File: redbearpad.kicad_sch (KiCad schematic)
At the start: 11 parts, among them J1 BlendMicro_fila_izq, J2 BlendMicro_fila_der, J3 OLED_128x32_I2C, SW1 Redragon_LP, SW2 Redragon_LP, SW3 Redragon_LP, SW4 Redragon_LP, SW5 Redragon_LP, SW6 Redragon_LP, SW7 Redragon_LP, SW8 Redragon_LP

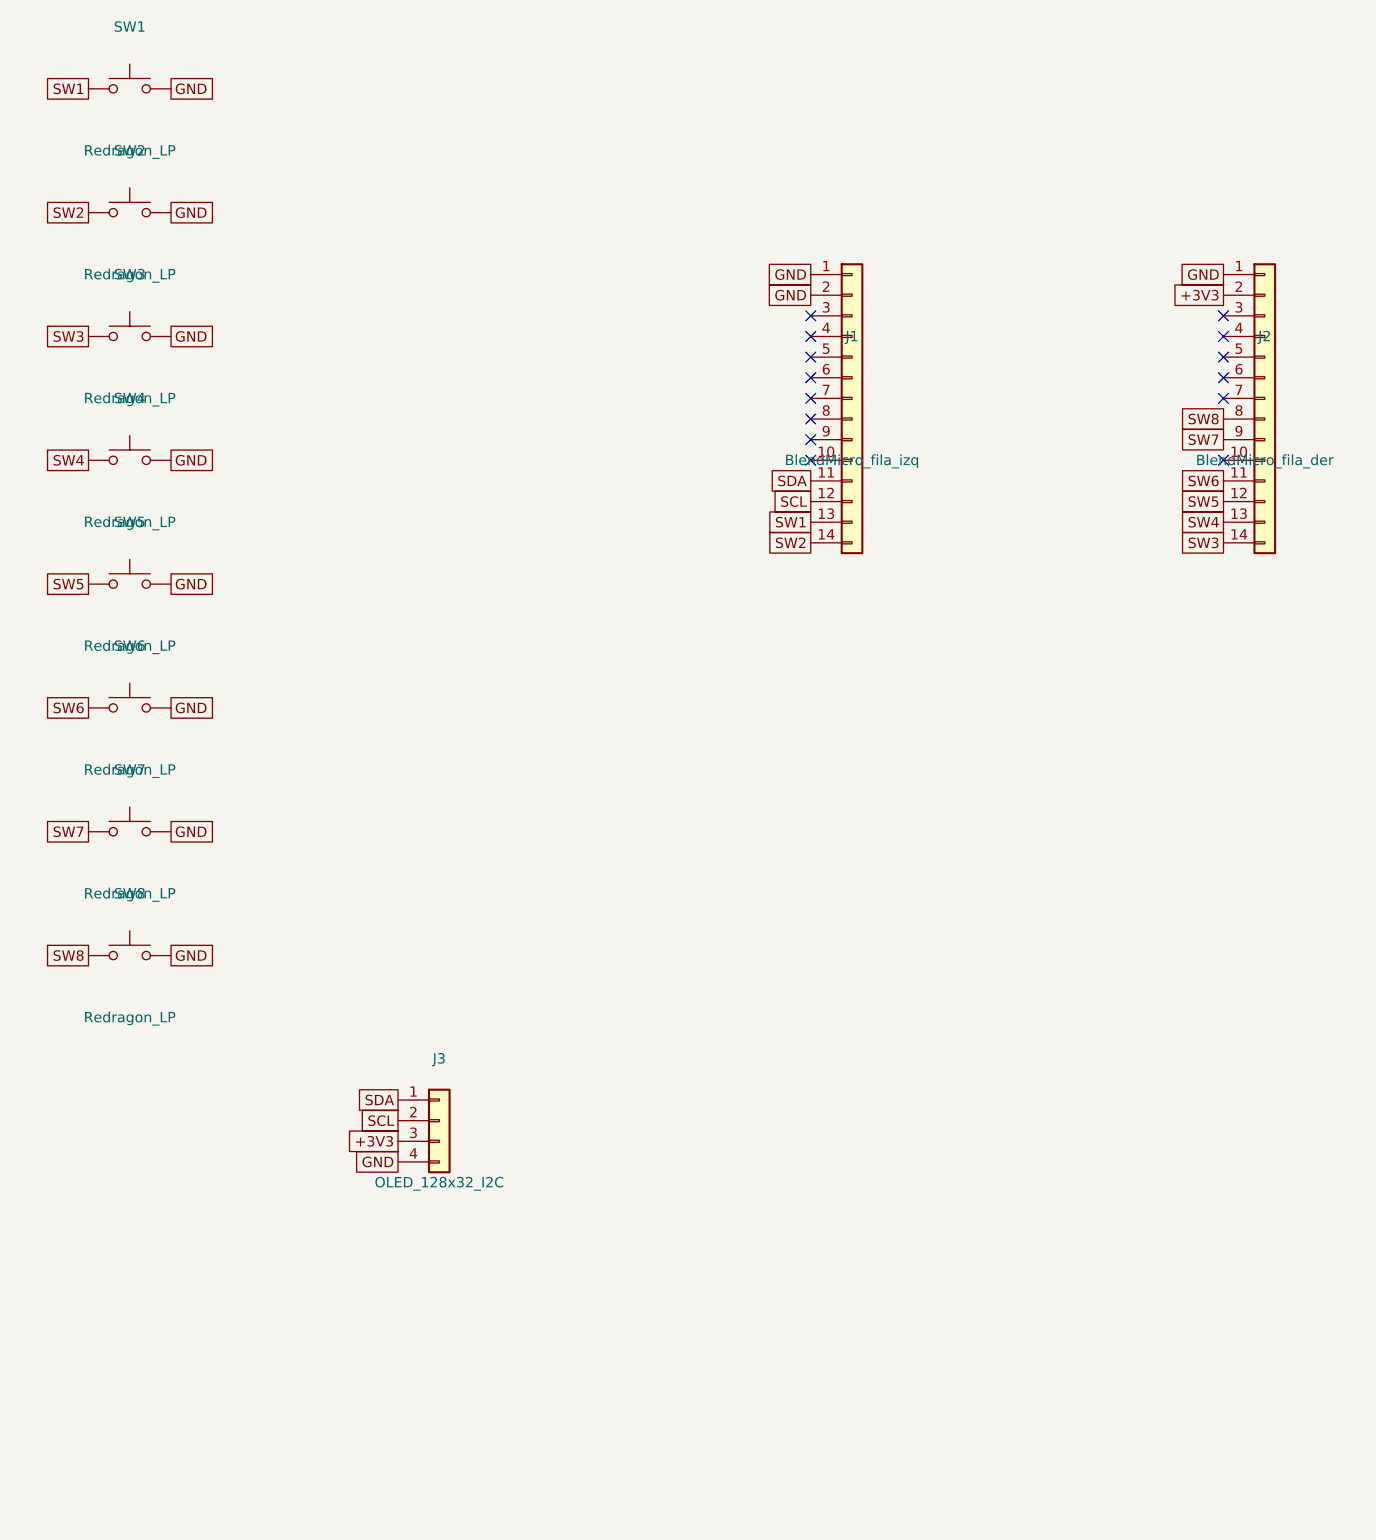
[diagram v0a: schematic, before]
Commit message: feat(pcb-v2): esquematico a 12 entradas (10 MX + 2 tact), OLED fuera
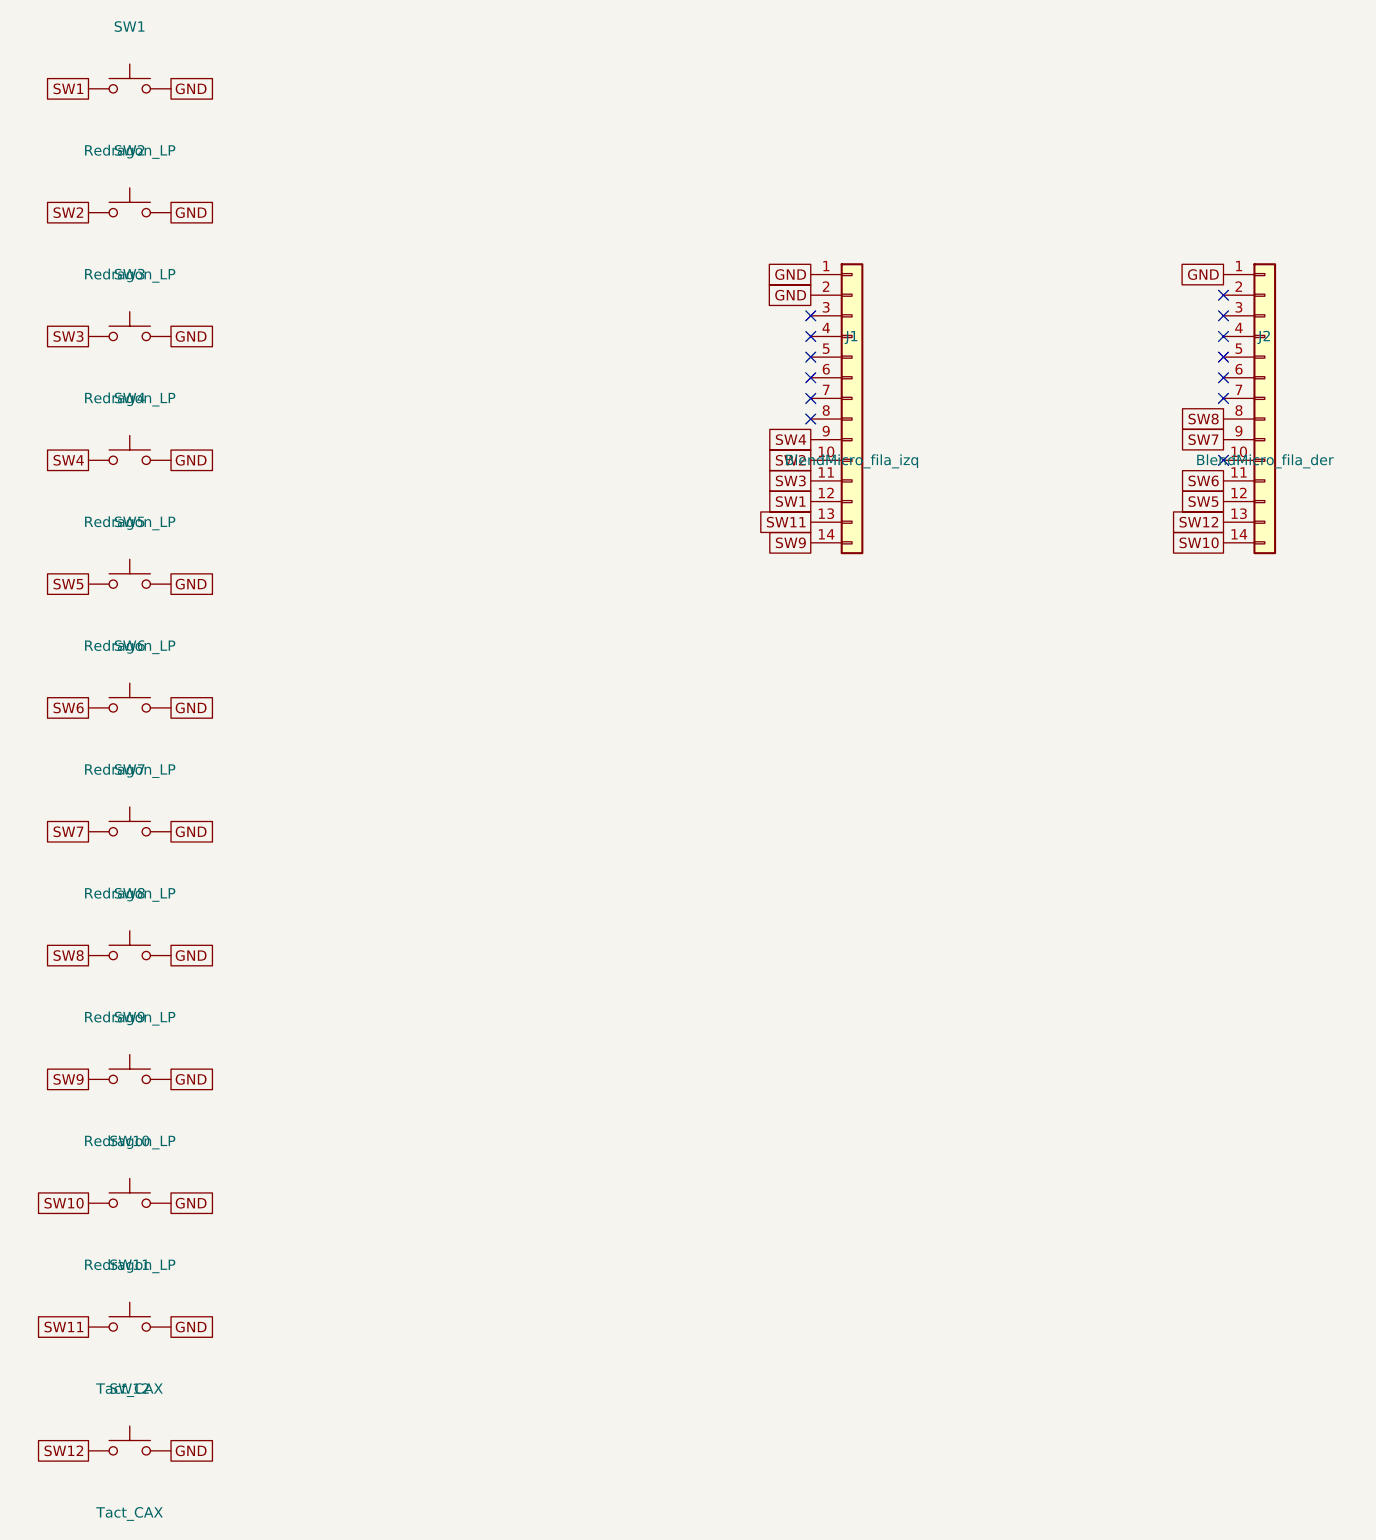
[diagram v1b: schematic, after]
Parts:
- removed J3: OLED_128x32_I2C, Connector_PinSocket_2.54mm:PinSocket_1x04_P2.54mm_Vertical, symbol Connector_Generic:Conn_01x04
- added SW10, SW9: Redragon_LP, redbearpad:SW_Redragon_LowProfile_PCB_1.00u, symbol Switch:SW_Push
- added SW11, SW12: Tact_CAX, redbearpad:SW_Tact_CAX_4.5x4.5, symbol Switch:SW_Push
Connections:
- net SCL is gone; now on net SW1: J1.12 (Pin_12)
- net SDA is gone; now on net SW3: J1.11 (Pin_11)
- net GND: now also SW10.2, SW11.2, SW12.2, SW9.2
- net SW1: no longer J1.13 (Pin_13)
- net SW2: now also J1.10 (Pin_10); no longer J1.14 (Pin_14)
- net SW3: no longer J2.14 (Pin_14)
- net SW4: now also J1.9 (Pin_9); no longer J2.13 (Pin_13)
- net +3V3: no longer names the net of J2.2 (Pin_2)
- new net SW10: J2.14 (Pin_14), SW10.1
- new net SW11: J1.13 (Pin_13), SW11.1
- new net SW12: J2.13 (Pin_13), SW12.1
- new net SW9: J1.14 (Pin_14), SW9.1
- no-connect marks 14 -> 13
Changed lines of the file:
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@@
   (global_label "SW8" (shape passive) (at 58.42 132.08 180) (effects (font (size 1.27 1.27)) (justify right)))
   (global_label "GND" (shape passive) (at 68.58 132.08 0) (effects (font (size 1.27 1.27)) (justify left)))
+  (symbol (lib_id "Switch:SW_Push") (at 63.5 147.32 0) (unit 1)
+    (exclude_from_sim no) (in_bom yes) (on_board yes) (dnp no)
+    (property "Reference" "SW9" (at 63.5 139.7 0) (effects (font (size 1.27 1.27))))
+    (property "Value" "Redragon_LP" (at 63.5 154.94 0) (effects (font (size 1.27 1.27))))
+    (property "Footprint" "redbearpad:SW_Redragon_LowProfile_PCB_1.00u" (at 63.5 147.32 0) (effects (font (size 1.27 1.27)) (hide yes)))
+    (property "Datasheet" "" (at 63.5 147.32 0) (effects (font (size 1.27 1.27)) (hide yes)))
+    (pin "1")
+    (pin "2")
+    (instances (project "redbearpad" (path "/f0a11111-2222-3333-4444-555566667777" (reference "SW9") (unit 1))))
+  )
+  (global_label "SW9" (shape passive) (at 58.42 147.32 180) (effects (font (size 1.27 1.27)) (justify right)))
+  (global_label "GND" (shape passive) (at 68.58 147.32 0) (effects (font (size 1.27 1.27)) (justify left)))
+  (symbol (lib_id "Switch:SW_Push") (at 63.5 162.56 0) (unit 1)
+    (exclude_from_sim no) (in_bom yes) (on_board yes) (dnp no)
+    (property "Reference" "SW10" (at 63.5 154.94 0) (effects (font (size 1.27 1.27))))
+    (property "Value" "Redragon_LP" (at 63.5 170.18 0) (effects (font (size 1.27 1.27))))
+    (property "Footprint" "redbearpad:SW_Redragon_LowProfile_PCB_1.00u" (at 63.5 162.56 0) (effects (font (size 1.27 1.27)) (hide yes)))
+    (property "Datasheet" "" (at 63.5 162.56 0) (effects (font (size 1.27 1.27)) (hide yes)))
+    (pin "1")
+    (pin "2")
+    (instances (project "redbearpad" (path "/f0a11111-2222-3333-4444-555566667777" (reference "SW10") (unit 1))))
+  )
+  (global_label "SW10" (shape passive) (at 58.42 162.56 180) (effects (font (size 1.27 1.27)) (justify right)))
+  (global_label "GND" (shape passive) (at 68.58 162.56 0) (effects (font (size 1.27 1.27)) (justify left)))
+  (symbol (lib_id "Switch:SW_Push") (at 63.5 177.8 0) (unit 1)
+    (exclude_from_sim no) (in_bom yes) (on_board yes) (dnp no)
+    (property "Reference" "SW11" (at 63.5 170.18 0) (effects (font (size 1.27 1.27))))
+    (property "Value" "Tact_CAX" (at 63.5 185.42000000000002 0) (effects (font (size 1.27 1.27))))
+    (property "Footprint" "redbearpad:SW_Tact_CAX_4.5x4.5" (at 63.5 177.8 0) (effects (font (size 1.27 1.27)) (hide yes)))
+    (property "Datasheet" "" (at 63.5 177.8 0) (effects (font (size 1.27 1.27)) (hide yes)))
+    (pin "1")
+    (pin "2")
+    (instances (project "redbearpad" (path "/f0a11111-2222-3333-4444-555566667777" (reference "SW11") (unit 1))))
+  )
+  (global_label "SW11" (shape passive) (at 58.42 177.8 180) (effects (font (size 1.27 1.27)) (justify right)))
+  (global_label "GND" (shape passive) (at 68.58 177.8 0) (effects (font (size 1.27 1.27)) (justify left)))
+  (symbol (lib_id "Switch:SW_Push") (at 63.5 193.04000000000002 0) (unit 1)
+    (exclude_from_sim no) (in_bom yes) (on_board yes) (dnp no)
+    (property "Reference" "SW12" (at 63.5 185.42000000000002 0) (effects (font (size 1.27 1.27))))
+    (property "Value" "Tact_CAX" (at 63.5 200.66000000000003 0) (effects (font (size 1.27 1.27))))
+    (property "Footprint" "redbearpad:SW_Tact_CAX_4.5x4.5" (at 63.5 193.04000000000002 0) (effects (font (size 1.27 1.27)) (hide yes)))
+    (property "Datasheet" "" (at 63.5 193.04000000000002 0) (effects (font (size 1.27 1.27)) (hide yes)))
+    (pin "1")
+    (pin "2")
+    (instances (project "redbearpad" (path "/f0a11111-2222-3333-4444-555566667777" (reference "SW12") (unit 1))))
+  )
+  (global_label "SW12" (shape passive) (at 58.42 193.04000000000002 180) (effects (font (size 1.27 1.27)) (justify right)))
+  (global_label "GND" (shape passive) (at 68.58 193.04000000000002 0) (effects (font (size 1.27 1.27)) (justify left)))
   (symbol (lib_id "Connector_Generic:Conn_01x14") (at 152.4 63.5 0) (unit 1)
     (exclude_from_sim no) (in_bom yes) (on_board yes) (dnp no)
@@
   (no_connect (at 147.32 63.5))
   (no_connect (at 147.32 66.04))
-  (no_connect (at 147.32 68.58))
-  (no_connect (at 147.32 71.12))
-  (global_label "SDA" (shape passive) (at 147.32 73.66 180) (effects (font (size 1.27 1.27)) (justify right)))
-  (global_label "SCL" (shape passive) (at 147.32 76.2 180) (effects (font (size 1.27 1.27)) (justify right)))
-  (global_label "SW1" (shape passive) (at 147.32 78.74 180) (effects (font (size 1.27 1.27)) (justify right)))
-  (global_label "SW2" (shape passive) (at 147.32 81.28 180) (effects (font (size 1.27 1.27)) (justify right)))
+  (global_label "SW4" (shape passive) (at 147.32 68.58 180) (effects (font (size 1.27 1.27)) (justify right)))
+  (global_label "SW2" (shape passive) (at 147.32 71.12 180) (effects (font (size 1.27 1.27)) (justify right)))
+  (global_label "SW3" (shape passive) (at 147.32 73.66 180) (effects (font (size 1.27 1.27)) (justify right)))
+  (global_label "SW1" (shape passive) (at 147.32 76.2 180) (effects (font (size 1.27 1.27)) (justify right)))
+  (global_label "SW11" (shape passive) (at 147.32 78.74 180) (effects (font (size 1.27 1.27)) (justify right)))
+  (global_label "SW9" (shape passive) (at 147.32 81.28 180) (effects (font (size 1.27 1.27)) (justify right)))
   (symbol (lib_id "Connector_Generic:Conn_01x14") (at 203.2 63.5 0) (unit 1)
     (exclude_from_sim no) (in_bom yes) (on_board yes) (dnp no)
@@
   )
   (global_label "GND" (shape passive) (at 198.11999999999998 48.26 180) (effects (font (size 1.27 1.27)) (justify right)))
-  (global_label "+3V3" (shape passive) (at 198.11999999999998 50.8 180) (effects (font (size 1.27 1.27)) (justify right)))
+  (no_connect (at 198.11999999999998 50.8))
   (no_connect (at 198.11999999999998 53.34))
   (no_connect (at 198.11999999999998 55.88))
@@
   (global_label "SW6" (shape passive) (at 198.11999999999998 73.66 180) (effects (font (size 1.27 1.27)) (justify right)))
   (global_label "SW5" (shape passive) (at 198.11999999999998 76.2 180) (effects (font (size 1.27 1.27)) (justify right)))
-  (global_label "SW4" (shape passive) (at 198.11999999999998 78.74 180) (effects (font (size 1.27 1.27)) (justify right)))
-  (global_label "SW3" (shape passive) (at 198.11999999999998 81.28 180) (effects (font (size 1.27 1.27)) (justify right)))
-  (symbol (lib_id "Connector_Generic:Conn_01x04") (at 101.6 152.4 0) (unit 1)
-    (exclude_from_sim no) (in_bom yes) (on_board yes) (dnp no)
-    (property "Reference" "J3" (at 101.6 144.78 0) (effects (font (size 1.27 1.27))))
-    (property "Value" "OLED_128x32_I2C" (at 101.6 160.02 0) (effects (font (size 1.27 1.27))))
-    (property "Footprint" "Connector_PinSocket_2.54mm:PinSocket_1x04_P2.54mm_Vertical" (at 101.6 152.4 0) (effects (font (size 1.27 1.27)) (hide yes)))
-    (property "Datasheet" "" (at 101.6 152.4 0) (effects (font (size 1.27 1.27)) (hide yes)))
-    (pin "1")
-    (pin "2")
-    (pin "3")
-    (pin "4")
-    (instances (project "redbearpad" (path "/f0a11111-2222-3333-4444-555566667777" (reference "J3") (unit 1))))
-  )
-  (global_label "SDA" (shape passive) (at 96.52 149.86 180) (effects (font (size 1.27 1.27)) (justify right)))
-  (global_label "SCL" (shape passive) (at 96.52 152.4 180) (effects (font (size 1.27 1.27)) (justify right)))
-  (global_label "+3V3" (shape passive) (at 96.52 154.94 180) (effects (font (size 1.27 1.27)) (justify right)))
-  (global_label "GND" (shape passive) (at 96.52 157.48000000000002 180) (effects (font (size 1.27 1.27)) (justify right)))
+  (global_label "SW12" (shape passive) (at 198.11999999999998 78.74 180) (effects (font (size 1.27 1.27)) (justify right)))
+  (global_label "SW10" (shape passive) (at 198.11999999999998 81.28 180) (effects (font (size 1.27 1.27)) (justify right)))
   (sheet_instances (path "/" (page "1")))
 )
